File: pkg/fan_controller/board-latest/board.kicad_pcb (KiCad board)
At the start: 4 copper layers, 84 x 36 mm, 89 parts, among them J1 FAN1, J10 AIR_TEMP, J11 WATER_TEMP, J12 FPANEL, J13 Conn_02x03_Odd_Even, J2 FAN2, J3 FAN3, J4 FAN4, J5 CPU, J6 PUMP, J7 POWER_IN, J8 USB_C_Receptacle_USB2.0, J9 WATER_FLOW, Q1 2N7002, Q2 2N7002, Q3 2N7002, Q4 2N7002, Q5 2N7002, Q6 2N7002, Q7 2N7002, Q8 2N7002, U1 RP2040, U2 AP2112K-3.3, U3 W25Q128JVS, Y1 12MHz

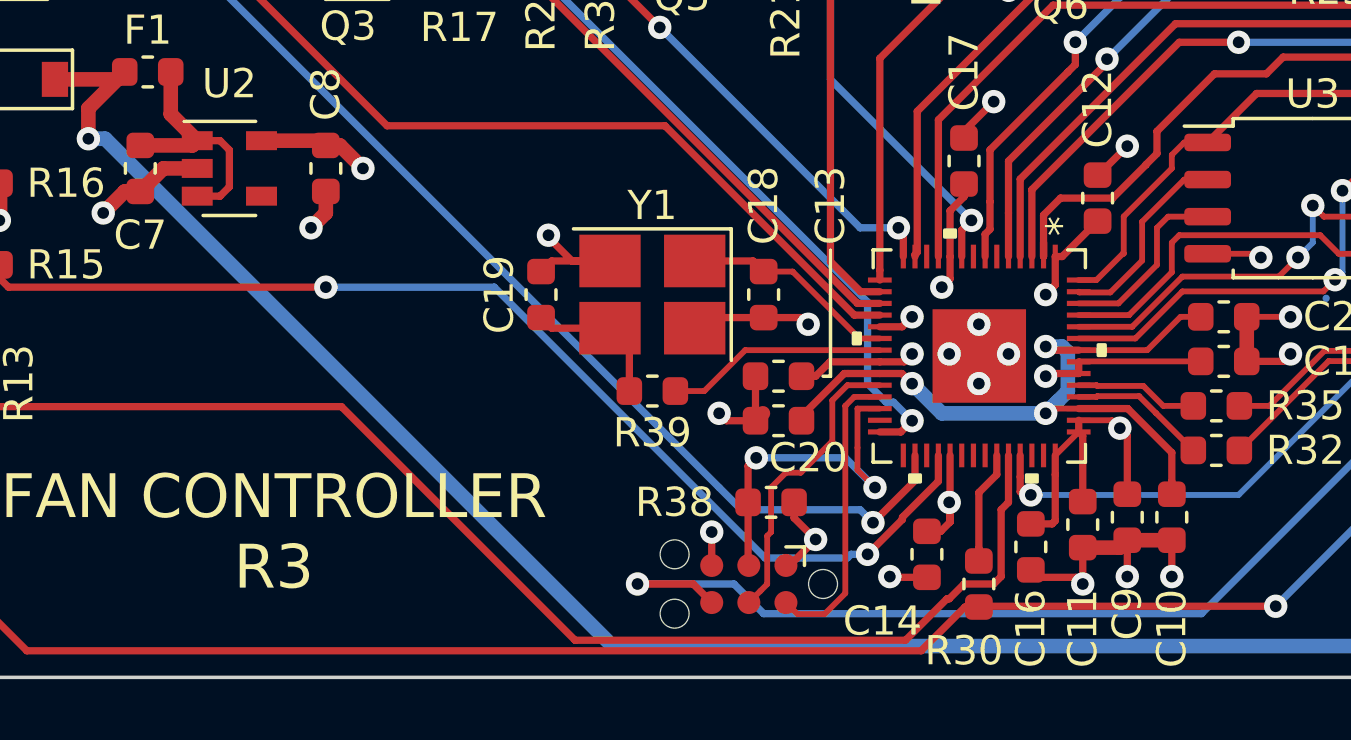
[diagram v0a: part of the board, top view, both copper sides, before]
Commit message: Clean up bugs and more testing.
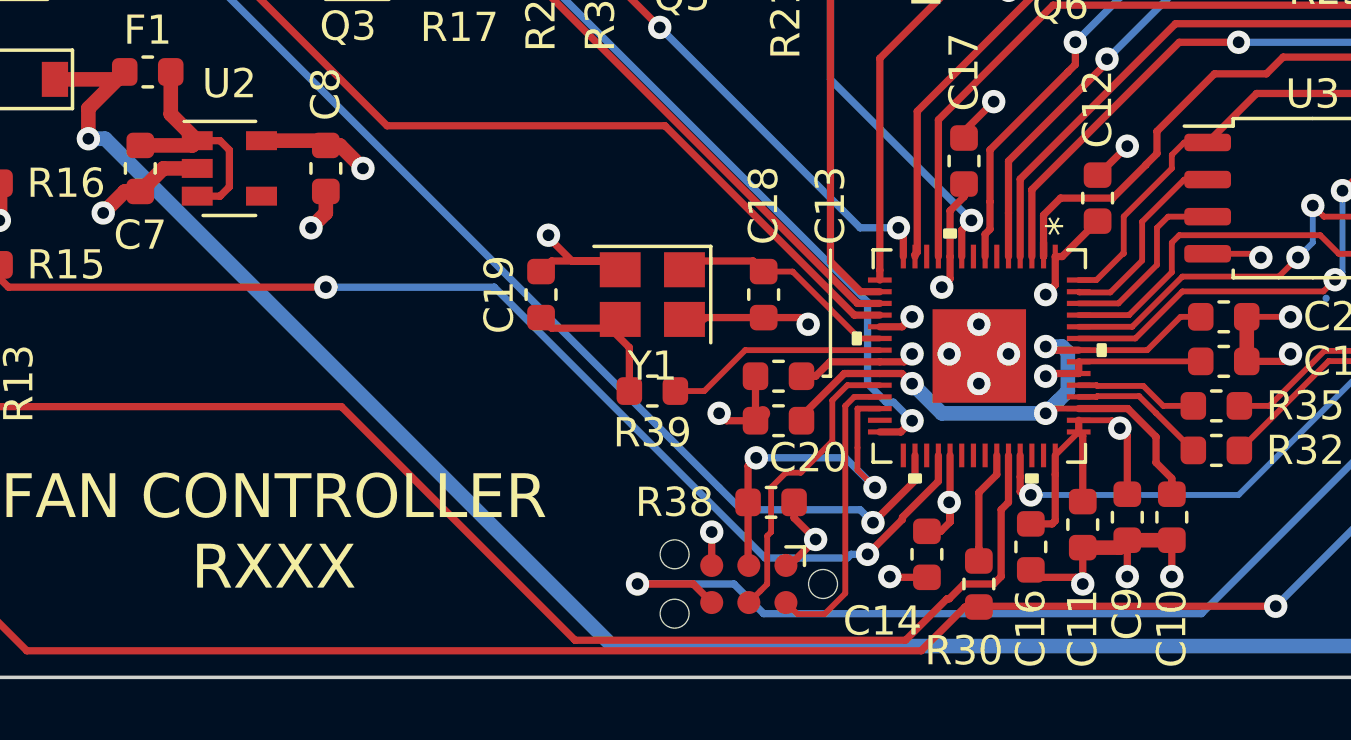
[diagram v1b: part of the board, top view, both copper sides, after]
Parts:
- Y1: footprint Crystal:Crystal_SMD_3225-4Pin_3.2x2.5mm_HandSoldering -> Crystal:Crystal_SMD_3225-4Pin_3.2x2.5mm
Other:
- board text added: "FAN CONTROLLER RXXX"
- board text removed: "FAN CONTROLLER R3"
